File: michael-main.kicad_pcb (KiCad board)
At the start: 2 copper layers, 121 parts, among them J1 CAN, J10 CAN, J11 Conn_01x05_Pin, J12 CAN, J13 Conn_01x03_Pin, J14 Conn_01x03_Pin, J15 Conn_01x03_Pin, J16 Conn_01x03_Pin, J2 USB_B_Mini, J3 Conn_01x05_Pin, J4 PPTC041LGBN-RC, J5 Conn_01x03_Pin, J6 Conn_01x05_Pin, J7 Conn_01x05_Pin, J8 CAN, J9 Conn_01x05_Pin, U1 STM32F446RETx, U10 LM1084-5.0, U11 MCP2551-I-SN, U12 MCP2551-I-SN, U13 MCP2551-I-SN, U2 STM32F446RETx, U3 STM32F446RETx, U4 STM32F446RETx, U5 STM32F446RETx, U6 MCP2551-I-SN, U7 USBLC6-4SC6, U8 BMI088, U9 LM1084-3.3, Y1 8Mhz, Y2 Crystal, Y3 Crystal, Y4 Crystal, Y5 Crystal

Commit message: updated estop circuit and buck converters for 16 and 6 volts, groups formed for pcb layout
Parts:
- added C37: 100u, Capacitor_SMD:C_Elec_10x10.2, F.Cu at (27.5, 23.0)
- added C39: 100u, Capacitor_SMD:C_Elec_10x10.2, F.Cu at (27.5, 34.9)
- added C40: 100u, Capacitor_SMD:C_Elec_10x10.2, F.Cu at (27.5, 46.7)
- added C42: 1n, Capacitor_SMD:C_0805_2012Metric, F.Cu at (27.0, 138.0)
- added C51: 1u, Capacitor_SMD:C_0805_2012Metric, F.Cu at (26.0, 134.0)
- added C52: 220u, Capacitor_SMD:C_Elec_6.3x7.7, F.Cu at (8.00, 71.0)
- added C53: 220u, Capacitor_SMD:C_Elec_6.3x7.7, F.Cu at (63.0, 102.0)
- added C54: 0.1u, Capacitor_SMD:C_0805_2012Metric, F.Cu at (38.0, 137.0)
- added C55: 10u, Capacitor_SMD:C_1206_3216Metric, F.Cu at (9.00, 77.0)
- added C56: 10u, Capacitor_SMD:C_1206_3216Metric, F.Cu at (57.0, 103.0)
- added C58: 0.1u, Capacitor_SMD:C_0805_2012Metric, F.Cu at (9.00, 81.0)
- added C59: 0.1u, Capacitor_SMD:C_0805_2012Metric, F.Cu at (53.0, 103.0)
- added C63: 0.1u, Capacitor_SMD:C_0805_2012Metric, F.Cu at (79.5, 107.0)
- added C64: 0.1u, Capacitor_SMD:C_0805_2012Metric, F.Cu at (27.0, 86.0)
- added C66: 0.1u, Capacitor_SMD:C_0805_2012Metric, F.Cu at (84.0, 107.0)
- added C67: 0.1u, Capacitor_SMD:C_0805_2012Metric, F.Cu at (27.0, 89.3)
- added C74: 0.1u, Capacitor_SMD:C_0805_2012Metric, F.Cu at (99.0, 100.0)
- added C75: 0.1u, Capacitor_SMD:C_0805_2012Metric, F.Cu at (43.0, 96.0)
- added C76: 220u, Capacitor_SMD:C_Elec_6.3x7.7, F.Cu at (43.0, 90.0)
- added C77: 220u, Capacitor_SMD:C_Elec_6.3x7.7, F.Cu at (93.0, 98.0)
- added D2: ss54, Diode_SMD:D_SMB, F.Cu at (36.0, 77.0)
- added D3: ss54, Diode_SMD:D_SMB, F.Cu at (82.0, 102.0)
- added D4: LED_Small, LED_SMD:LED_0805_2012Metric, F.Cu at (32.0, 89.0)
- added D5: LED_Small, LED_SMD:LED_0805_2012Metric, F.Cu at (105.8, 101.2)
- added H1: MountingHole, MountingHole:MountingHole_3.2mm_M3, F.Cu at (280.0, 132.0)
- added H2: MountingHole, MountingHole:MountingHole_3.2mm_M3, F.Cu at (279.8, 141.5)
- added H3: MountingHole, MountingHole:MountingHole_3.2mm_M3, F.Cu at (279.8, 149.4)
- added H4: MountingHole, MountingHole:MountingHole_3.2mm_M3, F.Cu at (279.8, 157.4)
- added J10: Conn_01x02_Pin, Connector_AMASS:AMASS_XT60PW-M_1x02_P7.20mm_Horizontal, F.Cu at (132.6, 150.8)
- added J11: Conn_01x02_Pin, Connector_AMASS:AMASS_XT60PW-M_1x02_P7.20mm_Horizontal, F.Cu at (109.8, 150.8)
- added J12: Conn_01x02_Pin, Connector_AMASS:AMASS_XT60PW-M_1x02_P7.20mm_Horizontal, F.Cu at (86.9, 150.8)
- added J13: Conn_01x02_Pin, Connector_AMASS:AMASS_XT60PW-M_1x02_P7.20mm_Horizontal, F.Cu at (64.0, 150.8)
- added J14: Conn_01x02_Pin, Connector_AMASS:AMASS_XT90PW-M_1x02_P10.90mm_Horizontal, F.Cu at (41.5, 44.5)
- added J15: Conn_01x02_Pin, Connector_PinHeader_2.54mm:PinHeader_1x02_P2.54mm_Vertical, F.Cu at (17.0, 135.2)
- added J22: Conn_01x02_Pin, Connector_AMASS:AMASS_XT60PW-M_1x02_P7.20mm_Horizontal, F.Cu at (45.9, 69.4)
- added L1: 6.8uH, Inductor_SMD:L_SXN_SMDRI124, F.Cu at (24.0, 72.0)
- added L2: 3uH, Inductor_SMD:L_Changjiang_FNR8040S, F.Cu at (81.0, 87.0)
- added Q1: BSC340N08NS3G, Package_TO_SOT_SMD:TDSON-8-1, F.Cu at (17.0, 107.3)
- added Q2: BSC340N08NS3G, Package_TO_SOT_SMD:TDSON-8-1, F.Cu at (17.0, 114.0)
- added Q3: BSC340N08NS3G, Package_TO_SOT_SMD:TDSON-8-1, F.Cu at (17.0, 120.7)
- added Q4: BSC340N08NS3G, Package_TO_SOT_SMD:TDSON-8-1, F.Cu at (17.0, 127.4)
- added R11: 10k, Resistor_SMD:R_0805_2012Metric, F.Cu at (22.0, 135.0)
- added R12: 1m, Resistor_SMD:R_2512_6332Metric, F.Cu at (31.0, 129.0)
- added R14: 24k, Resistor_SMD:R_0805_2012Metric, F.Cu at (9.00, 84.0)
- added R15: 24k, Resistor_SMD:R_0805_2012Metric, F.Cu at (71.0, 100.0)
- added R16: 100k, Resistor_SMD:R_0805_2012Metric, F.Cu at (24.0, 138.0)
- added R17: 0, Resistor_SMD:R_0805_2012Metric, F.Cu at (24.2, 129.7)
- added R18: 0, Resistor_SMD:R_0805_2012Metric, F.Cu at (24.2, 123.7)
- added R19: 5, Resistor_SMD:R_0805_2012Metric, F.Cu at (24.2, 126.7)
- added R23: 380k, Resistor_SMD:R_0805_2012Metric, F.Cu at (23.0, 86.0)
- added R24: 20k, Resistor_SMD:R_0805_2012Metric, F.Cu at (23.0, 89.0)
- added R25: 140k, Resistor_SMD:R_0805_2012Metric, F.Cu at (84.0, 94.0)
- added R26: 20k, Resistor_SMD:R_0805_2012Metric, F.Cu at (84.0, 97.0)
- added R27: 2.5k, Resistor_SMD:R_0805_2012Metric, F.Cu at (32.0, 86.2)
- added R28: 750, Resistor_SMD:R_0805_2012Metric, F.Cu at (106.0, 97.0)
- added U11: LMR14050SDDAR, Package_SO:Texas_HSOP-8-1EP_3.9x4.9mm_P1.27mm_ThermalVias, F.Cu at (16.1, 82.1)
- added U12: LMR14050SDDAR, Package_SO:Texas_HSOP-8-1EP_3.9x4.9mm_P1.27mm_ThermalVias, F.Cu at (74.7, 95.7)
- added U8: LTC7000EMSE-1_TRPBF, ltc7000emse:SOP50P490X110-17N, F.Cu at (32.4, 135.4)
- moved U13 169.3 mm to (257.0, 92.0)
- moved U1 169.1 mm to (257.0, 51.0)
- moved U2 163.7 mm to (276.5, 64.5)
- moved Y5 159.1 mm to (255.8, 104.7)
- moved Y1 153.6 mm to (253.1, 62.4)
- moved J4 150.9 mm to (267.0, 54.7)
- moved U15 148.5 mm to (259.5, 112.8)
- moved R22 147.1 mm to (269.5, 118.8)
- moved J1 142.3 mm to (253.5, 34.2)
- moved J19 139.9 mm to (277.5, 86.0)
- moved J21 139.9 mm to (277.5, 95.7)
- moved C65 138.6 mm to (244.6, 115.8)
- moved C22 137.8 mm to (278.8, 56.8)
- moved R3 137.8 mm to (274.4, 56.8)
- moved R4 137.8 mm to (274.4, 59.8)
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- renumbered C20 to C1, C23 to C10, C56 to C11, C4 to C12, C9 to C13, C15 to C14, C5 to C15, C24 to C16, C10 to C17, C11 to C18, C25 to C19, C6 to C2, C12 to C20, C26 to C21, C1 to C22, C13 to C23, C27 to C24, C14 to C25, C28 to C26, C29 to C27, C63 to C28, C57 to C29, C21 to C3, C58 to C31, C31 to C32, C32 to C33, C16 to C34, C33 to C35, C34 to C36, C35 to C38, C7 to C4, C52 to C41, C38 to C43, C39 to C44, C40 to C45, C64 to C46, C59 to C47, C41 to C48, C60 to C49, C2 to C5, C42 to C50, C44 to C57, C22 to C6, C45 to C60, C46 to C61, C53 to C62, C36 to C65, C37 to C68, C43 to C69, C55 to C7, C65 to C70, C61 to C71, C47 to C72, C62 to C73, C48 to C78, C17 to C79, C49 to C80, C50 to C81, C18 to C82, C51 to C83, C19 to C84, C54 to C85, C3 to C9, FB2 to FB1, FB1 to FB2, J13 to J1, J8 to J16, J15 to J17, J9 to J18, J16 to J19, J4 to J2, J10 to J20, J11 to J21, J12 to J24, J5 to J3, J6 to J4, J3 to J5, J1 to J6, J14 to J7, J2 to J8, J7 to J9, R3 to R1, R9 to R10, R15 to R13, R7 to R2, R10 to R20, R11 to R21, R16 to R22, R12 to R29, R1 to R3, R13 to R30, R2 to R4, R4 to R5, R5 to R6, R6 to R7, R14 to R8, R8 to R9, U2 to U1, U12 to U10, U5 to U13, U10 to U14, U13 to U15, U9 to U16, U6 to U2, U1 to U3, U8 to U4, U7 to U5, U3 to U6, U11 to U7, U4 to U9, Y2 to Y1, Y1 to Y2
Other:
- copper layers 2 -> 4

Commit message: finished componetnes placement, now need to add traces and pours
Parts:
- removed C34: 0.1uF, Capacitor_SMD:C_0603_1608Metric
- removed C37, C39, C40: 100u, Capacitor_SMD:C_Elec_10x10.2
- removed J10, J11, J12, J13: Conn_01x02_Pin, Connector_AMASS:AMASS_XT60PW-M_1x02_P7.20mm_Horizontal
- removed J16, J20, J24, J6: CAN, Connector_JST:JST_GH_BM02B-GHS-TBT_1x02-1MP_P1.25mm_Vertical
- removed U4: BMI088, bmi088:PQFN50P450X300X100-16N
- added J25: Conn_01x09_Socket, Connector_PinSocket_1.27mm:PinSocket_1x09_P1.27mm_Vertical, F.Cu at (70.0, 90.1)
- added J27: Conn_01x07_Socket, Connector_PinSocket_1.27mm:PinSocket_1x07_P1.27mm_Vertical, F.Cu at (87.8, 90.1)
- added J28: XT30PW_2_2_-M.G.B, xt302+2:AMASS_XT30PW_2_2_-M.G.B, F.Cu at (51.7, 162.8)
- added J29: XT30PW_2_2_-M.G.B, xt302+2:AMASS_XT30PW_2_2_-M.G.B, F.Cu at (68.8, 162.7)
- added J30: XT30PW_2_2_-M.G.B, xt302+2:AMASS_XT30PW_2_2_-M.G.B, F.Cu at (85.2, 162.7)
- added J31: XT30PW_2_2_-M.G.B, xt302+2:AMASS_XT30PW_2_2_-M.G.B, F.Cu at (102.2, 162.5)
- moved D4 243.4 mm to (269.7, 141.5)
- moved R27 243.3 mm to (269.7, 138.2)
- moved H3 241.1 mm to (39.2, 165.0)
- moved H4 233.6 mm to (70.5, 53.8)
- moved C22 182.9 mm to (118.4, 144.8), turned to 180 degrees
- moved U2 181.3 mm to (112.4, 141.6)
- moved R3 177.0 mm to (118.4, 140.4)
- moved R4 176.6 mm to (118.4, 142.6), turned to 180 degrees
- moved H1 166.7 mm to (134.0, 51.5)
- moved J1 165.1 mm to (123.0, 135.3)
- moved C73 164.0 mm to (102.6, 100.0), turned to 180 degrees
- moved J4 161.5 mm to (127.0, 135.2)
- moved C71 160.7 mm to (105.8, 100.0)
- moved R22 158.9 mm to (111.0, 107.6), turned to 90 degrees
- moved J19 158.5 mm to (122.8, 120.4)
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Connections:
- C28 pad 2: Net-(U6-NRST) -> /NRST2
- C46 pad 2: Net-(U9-NRST) -> /NRST3
- C5 pad 2: Net-(U1-NRST) -> /NRST1
- C52 pad 1: +24V -> +BATT
- C53 pad 1: +24V -> +BATT
- C54 pad 2: Net-(U8-TS) -> +24V
- C55 pad 1: +24V -> +BATT
- C56 pad 1: +24V -> +BATT
- C58 pad 1: +24V -> +BATT
- C59 pad 1: +24V -> +BATT
- C70 pad 2: Net-(U13-NRST) -> /NRST4
- J14 pad 2: +24V -> +BATT
- Q1 pad 1: Net-(U8-TS) -> +24V
- Q1 pad 2: Net-(U8-TS) -> +24V
- Q1 pad 3: Net-(U8-TS) -> +24V
- Q1 pad 5: Net-(Q1-D) -> /sen-
- Q2 pad 1: Net-(U8-TS) -> +24V
- Q2 pad 2: Net-(U8-TS) -> +24V
- Q2 pad 3: Net-(U8-TS) -> +24V
- Q2 pad 5: Net-(Q1-D) -> /sen-
- Q3 pad 1: Net-(U8-TS) -> +24V
- Q3 pad 2: Net-(U8-TS) -> +24V
- Q3 pad 3: Net-(U8-TS) -> +24V
- Q3 pad 5: Net-(Q1-D) -> /sen-
- Q4 pad 1: Net-(U8-TS) -> +24V
- Q4 pad 2: Net-(U8-TS) -> +24V
- Q4 pad 3: Net-(U8-TS) -> +24V
- Q4 pad 5: Net-(Q1-D) -> /sen-
- R12 pad 1: Net-(U8-SNS-) -> /sen-
- U1 pad 46: unconnected-(U1-PA13-Pad46) -> /TMS1
- U1 pad 49: unconnected-(U1-PA14-Pad49) -> /TCK1
- U1 pad 7: Net-(U1-NRST) -> /NRST1
- U11 pad 2: +24V -> +BATT
- U12 pad 2: +24V -> +BATT
- U13 pad 46: unconnected-(U13-PA13-Pad46) -> /TMS4
- U13 pad 49: unconnected-(U13-PA14-Pad49) -> /TCK4
- U13 pad 7: Net-(U13-NRST) -> /NRST4
- U15 pad 5: /Vre4_CAN -> /Vref4_CAN
- U3 pad 9: /INT3 -> /INT2
- U6 pad 46: unconnected-(U6-PA13-Pad46) -> /TMS2
- U6 pad 49: unconnected-(U6-PA14-Pad49) -> /TCK2
- U6 pad 7: Net-(U6-NRST) -> /NRST2
- U8 pad 11: Net-(U8-TS) -> +24V
- U8 pad 14: Net-(U8-SNS-) -> /sen-
- U9 pad 46: unconnected-(U9-PA13-Pad46) -> /TMS3
- U9 pad 49: unconnected-(U9-PA14-Pad49) -> /TCK3
- U9 pad 7: Net-(U9-NRST) -> /NRST3
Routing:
- net GND: track 0.00 -> 44.1 mm, vias 0 -> 13
- net +3.3V: track 0.00 -> 24.7 mm, vias 0 -> 1
- net +3.3VA: track 0.00 -> 14.8 mm
- net Net-(U3-PH1): track 0.00 -> 9.23 mm
- net Net-(U3-PH0): track 0.00 -> 9.23 mm
- net Net-(U6-PH1): track 0.00 -> 8.35 mm
- net Net-(U6-PH0): track 0.00 -> 8.22 mm
- net Net-(U9-PH1): track 0.00 -> 7.77 mm
- net Net-(U9-PH0): track 0.00 -> 7.69 mm
- net /SCK_SCL: track 0.00 -> 7.45 mm, vias 0 -> 2
- net Net-(U8-BST): track 0.00 -> 6.65 mm
- net /SDI_SDA: track 0.00 -> 6.24 mm, vias 0 -> 2
- net Net-(U8-TGDN): track 0.00 -> 5.32 mm
- net Net-(J15-Pin_1): track 0.00 -> 5.25 mm
- net Net-(U8-VCC): track 0.00 -> 5.23 mm
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
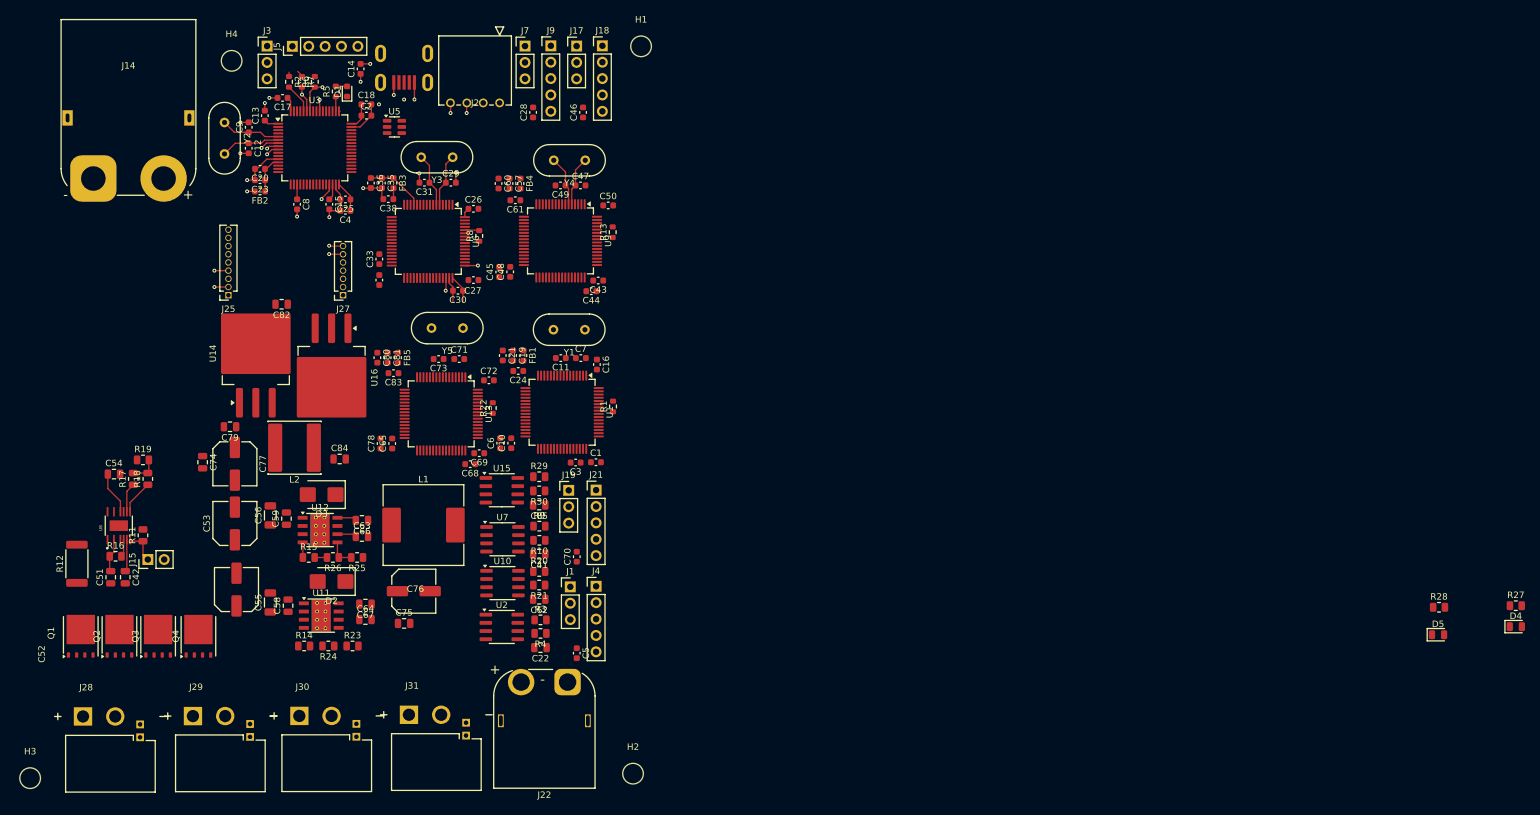
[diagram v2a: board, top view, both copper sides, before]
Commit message: finished all traces for pcb, including power and mcu sections. 1. need to look into 15V jetson power ripple (ldo) 2. pgnd and agnd seperation, star connection, 0 ohm connnection, or solder paste connection at front layer. 3. isolate osc sources 4. remove non-conducting layers for motor power lines front and back
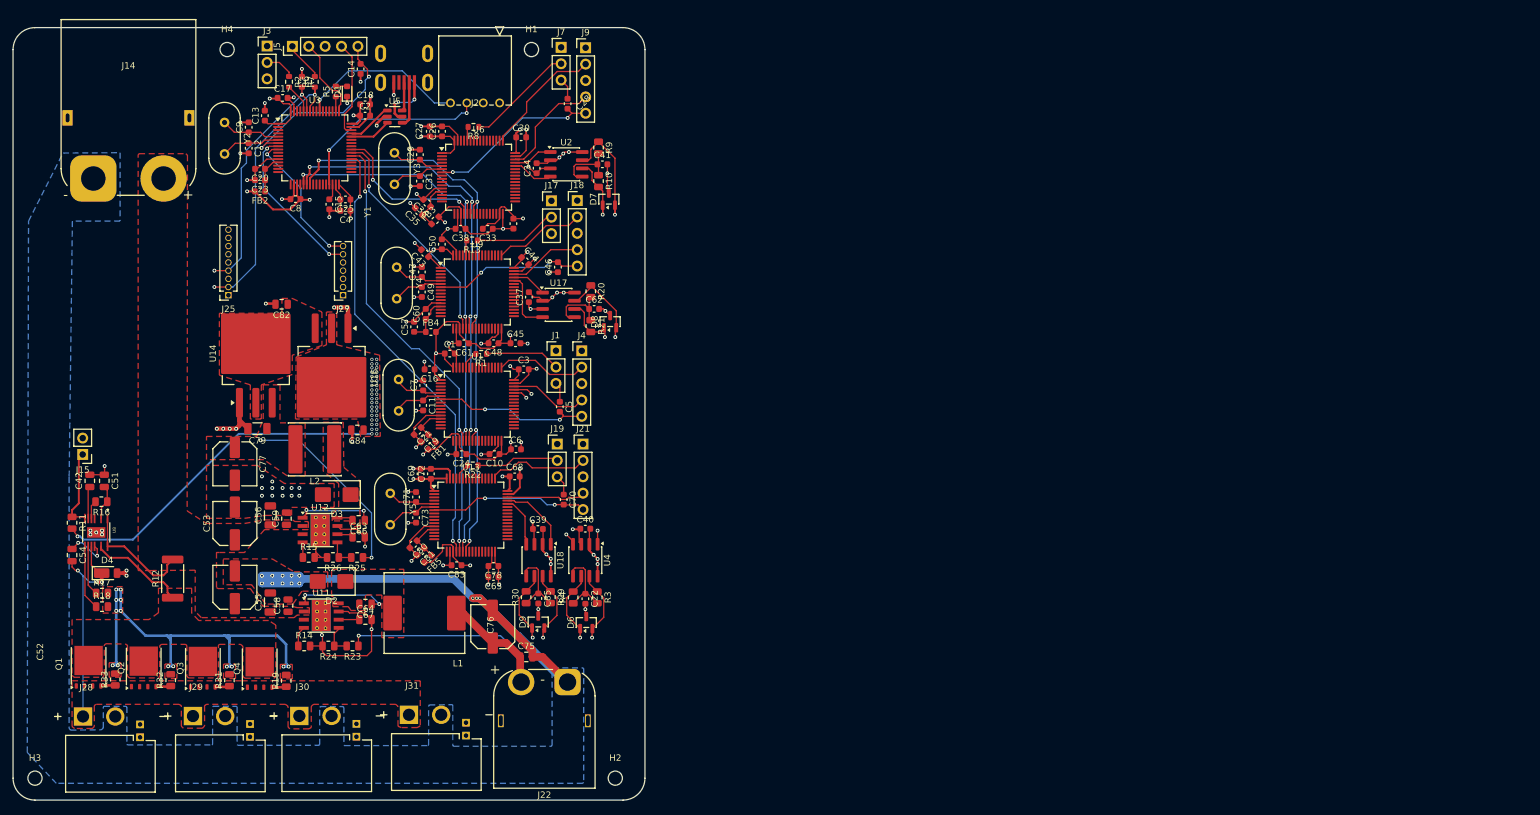
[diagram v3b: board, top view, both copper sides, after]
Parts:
- removed C74: 0.1u, Capacitor_SMD:C_0805_2012Metric
- removed D5: LED_Small, LED_SMD:LED_0805_2012Metric
- removed R27: 2.5k, Resistor_SMD:R_0805_2012Metric
- removed R28: 750, Resistor_SMD:R_0805_2012Metric
- removed U10, U15, U7: MCP2551-I-SN, Package_SO:SOIC-8_3.9x4.9mm_P1.27mm
- added C34: 0.1uF, Capacitor_SMD:C_0603_1608Metric, F.Cu at (117.8, 70.4)
- added C37: 0.1uF, Capacitor_SMD:C_0603_1608Metric, F.Cu at (116.6, 90.4)
- added C39: 0.1uF, Capacitor_SMD:C_0603_1608Metric, F.Cu at (118.0, 126.4)
- added C40: 0.1uF, Capacitor_SMD:C_0603_1608Metric, F.Cu at (125.3, 126.3)
- added D6: NUP2105L, Package_TO_SOT_SMD:SOT-23, F.Cu at (125.5, 140.9)
- added D7: NUP2105L, Package_TO_SOT_SMD:SOT-23, F.Cu at (129.0, 75.2)
- added D8: NUP2105L, Package_TO_SOT_SMD:SOT-23, F.Cu at (129.2, 94.2)
- added D9: NUP2105L, Package_TO_SOT_SMD:SOT-23, F.Cu at (118.0, 140.8)
- added R31: 5, Resistor_SMD:R_0805_2012Metric, F.Cu at (70.2, 149.8)
- added R32: 5, Resistor_SMD:R_0805_2012Metric, F.Cu at (61.0, 149.8)
- added R33: 5, Resistor_SMD:R_0805_2012Metric, F.Cu at (52.5, 149.7)
- added U17: SN65HVD230, Package_SO:SOIC-8_3.9x4.9mm_P1.27mm, F.Cu at (121.2, 91.6)
- added U18: SN65HVD230, Package_SO:SOIC-8_3.9x4.9mm_P1.27mm, F.Cu at (118.1, 131.2)
- added U4: SN65HVD230, Package_SO:SOIC-8_3.9x4.9mm_P1.27mm, F.Cu at (125.3, 131.2)
- C22, C41, C62, C85: value C_Small -> 47n; footprint Capacitor_SMD:C_0805_2012Metric -> Capacitor_SMD:C_0603_1608Metric
- C79: footprint Capacitor_SMD:C_0805_2012Metric -> Capacitor_SMD:C_1206_3216Metric
- D4: value LED_Small -> DFLS1150; footprint LED_SMD:LED_0805_2012Metric -> Diode_SMD:D_PowerDI-123
- H1, H2, H3, H4: footprint MountingHole:MountingHole_3.2mm_M3 -> MountingHole:MountingHole_2.2mm_M2
- U2: value MCP2551-I-SN -> SN65HVD230
- moved D4 218.6 mm to (51.2, 133.2)
- moved U2 72.4 mm to (122.4, 69.8)
- moved C41 61.2 mm to (128.0, 69.8), turned to 0 degrees
- moved R9 59.4 mm to (127.4, 67.2), turned to -90 degrees
- moved R10 56.5 mm to (127.4, 72.4), turned to -90 degrees
- moved C62 45.8 mm to (126.7, 92.2), turned to 0 degrees
- moved R20 44.2 mm to (126.2, 89.5), turned to -90 degrees
- moved R21 41.0 mm to (126.2, 94.9), turned to -90 degrees
- moved R19 40.8 mm to (79.0, 149.9), turned to 90 degrees
- moved C5 38.3 mm to (121.4, 107.4)
- moved J1 36.7 mm to (120.8, 98.7)
- moved J4 36.6 mm to (124.8, 98.7)
- moved Y4 33.6 mm to (96.1, 85.8), turned to -90 degrees
- moved FB5 31.5 mm to (101.0, 131.0), turned to -135 degrees
- moved C83 31.4 mm to (105.4, 132.0)
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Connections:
- C19 pad 1: +3.3VA -> +3.3VA2
- C20 pad 1: +3.3VA -> +3.3VA1
- C21 pad 1: +3.3VA -> +3.3VA2
- C22 pad 1: Net-(C22-Pad1) -> /Vref1_CAN
- C22 pad 2: /Vref1_CAN -> GND
- C23 pad 1: +3.3VA -> +3.3VA1
- C35 pad 1: +3.3VA -> +3.3VA3
- C36 pad 1: +3.3VA -> +3.3VA3
- C41 pad 1: Net-(C41-Pad1) -> /Vref2_CAN
- C41 pad 2: /Vref2_CAN -> GND
- C57 pad 1: +3.3VA -> +3.3VA4
- C60 pad 1: +3.3VA -> +3.3VA4
- C62 pad 1: Net-(C62-Pad1) -> /Vref3_CAN
- C62 pad 2: /Vref3_CAN -> GND
- C80 pad 1: +3.3VA -> +3.3V5
- C81 pad 1: +3.3VA -> +3.3V5
- C85 pad 1: Net-(C85-Pad1) -> /Vref4_CAN
- C85 pad 2: /Vref4_CAN -> GND
- D4 pad 1: GND -> +24V
- D4 pad 2: Net-(D4-A) -> GND
- FB1 pad 1: +3.3VA -> +3.3VA2
- FB2 pad 1: +3.3VA -> +3.3VA1
- FB3 pad 1: +3.3VA -> +3.3VA3
- FB4 pad 1: +3.3VA -> +3.3VA4
- FB5 pad 1: +3.3VA -> +3.3V5
- J28 pad S1: unconnected-(J28-PadS1) -> /CANH4
- J28 pad S2: unconnected-(J28-PadS2) -> /CANL4
- J29 pad S1: unconnected-(J29-PadS1) -> /CANH1
- J29 pad S2: unconnected-(J29-PadS2) -> /CANL1
- J30 pad S1: unconnected-(J30-PadS1) -> /CANH2
- J30 pad S2: unconnected-(J30-PadS2) -> /CANL2
- J31 pad S1: unconnected-(J31-PadS1) -> /CANH3
- J31 pad S2: unconnected-(J31-PadS2) -> /CANL3
- Q1 pad 4: Net-(Q1-G) -> /G1
- Q2 pad 4: Net-(Q1-G) -> /G2
- Q3 pad 4: Net-(Q1-G) -> /G3
- Q4 pad 4: Net-(Q1-G) -> /G4
- R10 pad 1: Net-(C41-Pad1) -> /Vref2_CAN
- R10 pad 2: Net-(U7-CANL) -> /CANL2
- R19 pad 1: Net-(Q1-G) -> /G4
- R20 pad 1: Net-(U10-CANH) -> /CANH3
- R20 pad 2: Net-(C62-Pad1) -> /Vref3_CAN
- R21 pad 1: Net-(C62-Pad1) -> /Vref3_CAN
- R21 pad 2: Net-(U10-CANL) -> /CANL3
- R29 pad 1: Net-(U15-CANH) -> /CANH4
- R29 pad 2: Net-(C85-Pad1) -> /Vref4_CAN
- R3 pad 1: Net-(U2-CANH) -> /CANH1
- R3 pad 2: Net-(C22-Pad1) -> /Vref1_CAN
- R30 pad 1: Net-(C85-Pad1) -> /Vref4_CAN
- R30 pad 2: Net-(U15-CANL) -> /CANL4
- R4 pad 1: Net-(C22-Pad1) -> /Vref1_CAN
- R4 pad 2: Net-(U2-CANL) -> /CANL1
- R9 pad 1: Net-(U7-CANH) -> /CANH2
- R9 pad 2: Net-(C41-Pad1) -> /Vref2_CAN
- U1 pad 13: +3.3VA -> +3.3VA2
- U1 pad 20: unconnected-(U1-PA4-Pad20) -> /CS2
- U1 pad 21: unconnected-(U1-PA5-Pad21) -> /SPI_SCK
- U1 pad 22: unconnected-(U1-PA6-Pad22) -> /SPI_MISO
- U1 pad 23: unconnected-(U1-PA7-Pad23) -> /SPI_MOSI
- U1 pad 44: unconnected-(U1-PA11-Pad44) -> /CAN1_RX
- U1 pad 45: unconnected-(U1-PA12-Pad45) -> /CAN1_TX
- U13 pad 13: +3.3VA -> +3.3V5
- U13 pad 20: unconnected-(U13-PA4-Pad20) -> /CS3
- U13 pad 21: unconnected-(U13-PA5-Pad21) -> /SPI_SCK
- U13 pad 22: unconnected-(U13-PA6-Pad22) -> /SPI_MISO
- U13 pad 23: unconnected-(U13-PA7-Pad23) -> /SPI_MOSI
- U13 pad 44: unconnected-(U13-PA11-Pad44) -> /CAN4_RX
- U13 pad 45: unconnected-(U13-PA12-Pad45) -> /CAN4_TX
- U14 pad 4: (no net) -> +5V
- U16 pad 4: (no net) -> +3.3V
- U2 pad 1: unconnected-(U2-TXD-Pad1) -> /CAN2_TX
- U2 pad 3: +5V -> +3.3V
- U2 pad 4: unconnected-(U2-RXD-Pad4) -> /CAN2_RX
- U2 pad 5: /Vref1_CAN -> /Vref2_CAN
- U2 pad 6: Net-(U2-CANL) -> /CANL2
- U2 pad 7: Net-(U2-CANH) -> /CANH2
- U3 pad 13: +3.3VA -> +3.3VA1
- U3 pad 20: unconnected-(U3-PA4-Pad20) -> /SPI_NSS
- U3 pad 21: unconnected-(U3-PA5-Pad21) -> /SPI_SCK
- U3 pad 22: unconnected-(U3-PA6-Pad22) -> /SPI_MISO
- U3 pad 23: /V_shunt_read -> /SPI_MOSI
- U3 pad 37: unconnected-(U3-PC6-Pad37) -> /CS3
- U3 pad 38: unconnected-(U3-PC7-Pad38) -> /CS2
- U3 pad 39: unconnected-(U3-PC8-Pad39) -> /CS1
- U3 pad 40: unconnected-(U3-PC9-Pad40) -> /CS0
- U6 pad 13: +3.3VA -> +3.3VA3
- U6 pad 20: unconnected-(U6-PA4-Pad20) -> /CS0
- U6 pad 21: unconnected-(U6-PA5-Pad21) -> /SPI_SCK
- U6 pad 22: unconnected-(U6-PA6-Pad22) -> /SPI_MISO
- U6 pad 23: unconnected-(U6-PA7-Pad23) -> /SPI_MOSI
- U6 pad 44: unconnected-(U6-PA11-Pad44) -> /CAN2_RX
- U6 pad 45: unconnected-(U6-PA12-Pad45) -> /CAN2_TX
- U9 pad 13: +3.3VA -> +3.3VA4
- U9 pad 20: unconnected-(U9-PA4-Pad20) -> /CS1
- U9 pad 21: unconnected-(U9-PA5-Pad21) -> /SPI_SCK
- U9 pad 22: unconnected-(U9-PA6-Pad22) -> /SPI_MISO
- U9 pad 23: unconnected-(U9-PA7-Pad23) -> /SPI_MOSI
- U9 pad 44: unconnected-(U9-PA11-Pad44) -> /CAN3_RX
- U9 pad 45: unconnected-(U9-PA12-Pad45) -> /CAN3_TX
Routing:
- net GND: track 44.1 -> 367.9 mm, vias 13 -> 106
- net +3.3V: track 24.7 -> 238.2 mm, vias 1 -> 61
- net /CANH2: track 0.00 -> 143.7 mm, vias 0 -> 1
- net /CANL2: track 0.00 -> 134.1 mm, vias 0 -> 1
- net /SPI_MOSI: track 0.00 -> 93.7 mm, vias 0 -> 5
- net /CANH3: track 0.00 -> 93.0 mm, vias 0 -> 1
- net /SPI_MISO: track 0.00 -> 91.3 mm, vias 0 -> 5
- net /SPI_SCK: track 0.00 -> 89.1 mm, vias 0 -> 5
- net /CANL3: track 0.00 -> 86.9 mm, vias 0 -> 1
- net /CANH4: track 0.00 -> 80.3 mm, vias 0 -> 1
- net /CANL4: track 0.00 -> 77.9 mm, vias 0 -> 1
- net /CANH1: track 0.00 -> 74.8 mm, vias 0 -> 1
- net /CANL1: track 0.00 -> 72.6 mm, vias 0 -> 1
- net /CS3: track 0.00 -> 69.1 mm, vias 0 -> 2
- net Net-(R17-Pad2): track 4.35 -> 66.5 mm, vias 0 -> 14
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- added copper zone on F.Cu, net +24V
- added copper zone on F.Cu, net +3.3V
- added copper zone on In2.Cu, net +3.3V
- added copper zone on F.Cu, net +5V
- added copper zone on F.Cu, net +6V
- added copper zone on F.Cu, net +BATT
- added copper zone on F.Cu, net /sen-
- added copper zone on B.Cu, net GND
- added copper zone on F.Cu, net GND
- added copper zone on In1.Cu, net GND
- added copper zone on F.Cu, net Net-(D2-K)
- added copper zone on F.Cu, net Net-(D3-K)
- added copper zone on F.Cu, net Net-(R17-Pad2)
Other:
- board outline added: 98 x 119.8 mm
